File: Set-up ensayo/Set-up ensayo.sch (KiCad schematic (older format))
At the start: 14 parts, among them J1 Conn_Coaxial, J2 DB9_Female_MountingHoles

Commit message: Terminé con el 3er paso del proceso de diseño de esquemático. Cada componente tiene su footprint pero hay que vericarlo
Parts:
- H1, H2, H3, H4: footprint (none) -> MountingHole:MountingHole_2.2mm_M2_ISO7380_Pad
- J1: footprint (none) -> Connector_Coaxial:BNC_TEConnectivity_1478204_Vertical
- J2: footprint (none) -> Connector_Dsub:DSUB-9_Female_Horizontal_P2.77x2.84mm_EdgePinOffset4.94mm_Housed_MountingHolesOffset7.48mm
- MCB1: footprint (none) -> digikey-footprints:Switch_Toggle_ATE1D-2M3-10-Z
- R1: footprint (none) -> Resistor_THT:R_Axial_DIN0204_L3.6mm_D1.6mm_P5.08mm_Horizontal
- TP1, TP2, TP3, TP4, TP5, TP6: footprint (none) -> Connector_PinHeader_1.00mm:PinHeader_1x01_P1.00mm_Horizontal
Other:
- note added: "Pto. medición osciloscopio V1"
- note added: "Pto. medición osciloscopio V2"
- note removed: "Pto. medición osciloscopio"
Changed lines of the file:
@@
 F 0 "H1" H 1300 2799 50  0000 L CNN
 F 1 "MountingHole_Pad" H 1300 2708 50  0000 L CNN
-F 2 "" H 1200 2750 50  0001 C CNN
+F 2 "MountingHole:MountingHole_2.2mm_M2_ISO7380_Pad" H 1200 2750 50  0001 C CNN
 F 3 "~" H 1200 2750 50  0001 C CNN
 F 4 "Fijación e interfaz eléctrica con chasis" H 1200 2750 50  0001 C CNN "Función"
@@
 F 0 "H3" H 8400 2849 50  0000 L CNN
 F 1 "MountingHole_Pad" H 8400 2758 50  0000 L CNN
-F 2 "" H 8300 2800 50  0001 C CNN
+F 2 "MountingHole:MountingHole_2.2mm_M2_ISO7380_Pad" H 8300 2800 50  0001 C CNN
 F 3 "~" H 8300 2800 50  0001 C CNN
 F 4 "Fijación e interfaz eléctrica con chasis" H 8300 2800 50  0001 C CNN "Función"
@@
 F 0 "H2" H 1300 5149 50  0000 L CNN
 F 1 "MountingHole_Pad" H 1300 5058 50  0000 L CNN
-F 2 "" H 1200 5100 50  0001 C CNN
+F 2 "MountingHole:MountingHole_2.2mm_M2_ISO7380_Pad" H 1200 5100 50  0001 C CNN
 F 3 "~" H 1200 5100 50  0001 C CNN
 F 4 "Fijación e interfaz eléctrica con chasis" H 1200 5100 50  0001 C CNN "Función"
@@
 F 0 "H4" H 8450 5199 50  0000 L CNN
 F 1 "MountingHole_Pad" H 8450 5108 50  0000 L CNN
-F 2 "" H 8350 5150 50  0001 C CNN
+F 2 "MountingHole:MountingHole_2.2mm_M2_ISO7380_Pad" H 8350 5150 50  0001 C CNN
 F 3 "~" H 8350 5150 50  0001 C CNN
 F 4 "Fijación e interfaz eléctrica con chasis" H 8350 5150 50  0001 C CNN "Función"
@@
 F 0 "J1" H 2200 3475 50  0000 L CNN
 F 1 "Conn_Coaxial" H 2200 3384 50  0000 L CNN
-F 2 "" H 2100 3500 50  0001 C CNN
+F 2 "Connector_Coaxial:BNC_TEConnectivity_1478204_Vertical" H 2100 3500 50  0001 C CNN
 F 3 " ~" H 2100 3500 50  0001 C CNN
 F 4 "Interfaz eléctrica con generador de señales" H 2100 3500 50  0001 C CNN "Función"
@@
 F 0 "MCB1" H 4950 3825 50  0000 C CNN
 F 1 "INT_1P2D" H 4950 3734 50  0000 C CNN
-F 2 "" H 4950 3500 50  0001 C CNN
+F 2 "digikey-footprints:Switch_Toggle_ATE1D-2M3-10-Z" H 4950 3500 50  0001 C CNN
 F 3 "" H 4950 3500 50  0001 C CNN
 F 4 "Interruptor HMI para cambio enter ajuste y ensayo" H 4950 3500 50  0001 C CNN "Función"
@@
 F 0 "R1" V 5757 3400 50  0000 C CNN
 F 1 "R" V 5666 3400 50  0000 C CNN
-F 2 "" V 5480 3400 50  0001 C CNN
+F 2 "Resistor_THT:R_Axial_DIN0204_L3.6mm_D1.6mm_P5.08mm_Horizontal" V 5480 3400 50  0001 C CNN
 F 3 "~" H 5550 3400 50  0001 C CNN
 F 4 "Resistencia de medición de sensor" V 5550 3400 50  0001 C CNN "Función"
@@
 F 0 "J2" H 7680 4052 50  0000 L CNN
 F 1 "DB9_Female_MountingHoles" H 7680 3961 50  0000 L CNN
-F 2 "" H 7500 4050 50  0001 C CNN
+F 2 "Connector_Dsub:DSUB-9_Female_Horizontal_P2.77x2.84mm_EdgePinOffset4.94mm_Housed_MountingHolesOffset7.48mm" H 7500 4050 50  0001 C CNN
 F 3 " ~" H 7500 4050 50  0001 C CNN
 F 4 "Interfaz eléctrica con sensores" H 7500 4050 50  0001 C CNN "Función"
@@
 F 0 "TP3" H 3853 4001 50  0000 L CNN
 F 1 "TestPoint_Probe" H 3853 3910 50  0000 L CNN
-F 2 "" H 3900 3900 50  0001 C CNN
+F 2 "Connector_PinHeader_1.00mm:PinHeader_1x01_P1.00mm_Horizontal" H 3900 3900 50  0001 C CNN
 F 3 "~" H 3900 3900 50  0001 C CNN
 F 4 "Interfaz eléctrica con punta de medición V1 osciloscopio" H 3700 3900 50  0001 C CNN "Función"
@@
 F 0 "TP5" H 6053 3951 50  0000 L CNN
 F 1 "TestPoint_Probe" H 6053 3860 50  0000 L CNN
-F 2 "" H 6100 3850 50  0001 C CNN
+F 2 "Connector_PinHeader_1.00mm:PinHeader_1x01_P1.00mm_Horizontal" H 6100 3850 50  0001 C CNN
 F 3 "~" H 6100 3850 50  0001 C CNN
 F 4 "Interfaz eléctrica con punta de medición V2 osciloscopio" H 5900 3850 50  0001 C CNN "Función"
@@
 F 0 "TP6" H 5958 4468 50  0000 L CNN
 F 1 "TestPoint" H 5958 4377 50  0000 L CNN
-F 2 "" H 6100 4350 50  0001 C CNN
+F 2 "Connector_PinHeader_1.00mm:PinHeader_1x01_P1.00mm_Horizontal" H 6100 4350 50  0001 C CNN
 F 3 "~" H 6100 4350 50  0001 C CNN
 F 4 "Interfaz eléctrica con GND de V2 osciloscopio" H 5900 4350 50  0001 C CNN "Función"
@@
 F 0 "TP4" H 3758 4418 50  0000 L CNN
 F 1 "TestPoint" H 3758 4327 50  0000 L CNN
-F 2 "" H 3900 4300 50  0001 C CNN
+F 2 "Connector_PinHeader_1.00mm:PinHeader_1x01_P1.00mm_Horizontal" H 3900 4300 50  0001 C CNN
 F 3 "~" H 3900 4300 50  0001 C CNN
 F 4 "Interfaz eléctrica con GND de V1 osciloscopio" H 3700 4300 50  0001 C CNN "Función"
@@
 F 0 "TP1" H 2908 4068 50  0000 L CNN
 F 1 "TestPoint_Alt" H 2908 3977 50  0000 L CNN
-F 2 "" H 3050 3950 50  0001 C CNN
+F 2 "Connector_PinHeader_1.00mm:PinHeader_1x01_P1.00mm_Horizontal" H 3050 3950 50  0001 C CNN
 F 3 "~" H 3050 3950 50  0001 C CNN
 F 4 "Interfaz eléctrica con potencial positivo tester" H 2850 3950 50  0001 C CNN "Función"
@@
 F 0 "TP2" H 2908 4468 50  0000 L CNN
 F 1 "TestPoint" H 2908 4377 50  0000 L CNN
-F 2 "" H 3050 4350 50  0001 C CNN
+F 2 "Connector_PinHeader_1.00mm:PinHeader_1x01_P1.00mm_Horizontal" H 3050 4350 50  0001 C CNN
 F 3 "~" H 3050 4350 50  0001 C CNN
 F 4 "Interfaz eléctrica con potencial negativo tester" H 2850 4350 50  0001 C CNN "Función"
@@
 Pto. medición tester
 Text Notes 3600 4600 0    50   ~ 0
-Pto. medición osciloscopio
+Pto. medición osciloscopio V1
 Text Notes 4600 3900 0    50   ~ 0
 Ensayo/Ajuste
 Text Notes 5600 4600 0    50   ~ 0
-Pto. medición osciloscopio
+Pto. medición osciloscopio V2
 Wire Notes Line
 	6950 3400 6950 4750

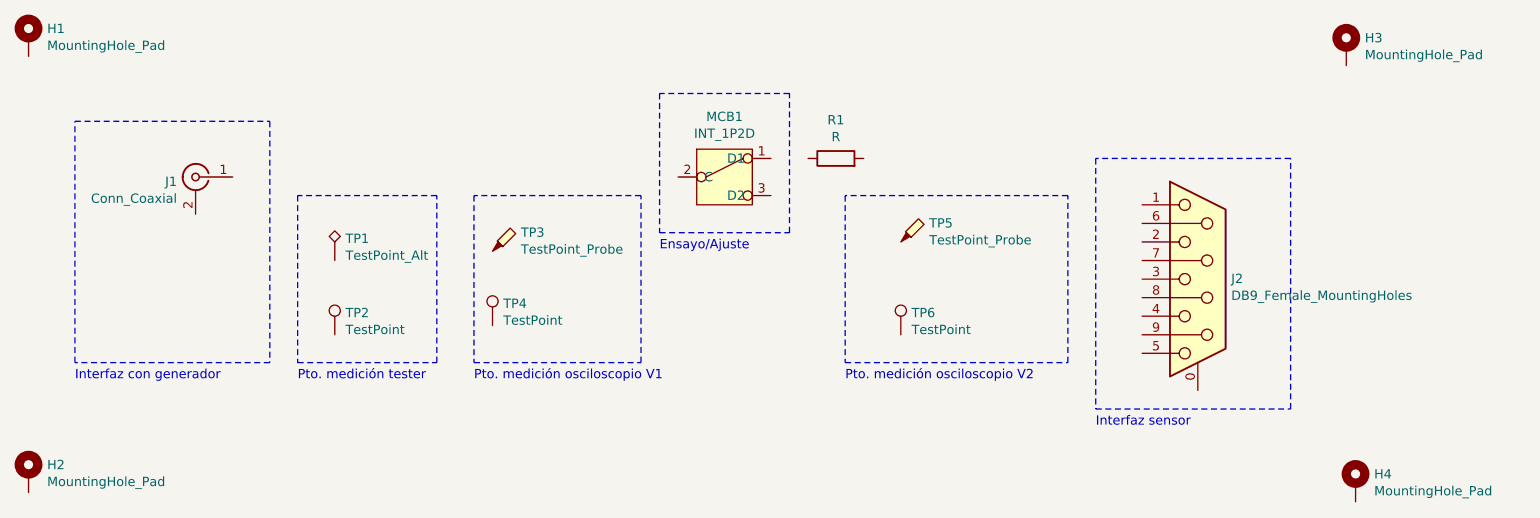
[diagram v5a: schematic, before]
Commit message: Pasos 4 y 5 del proceso de diseño de esquemático hechos
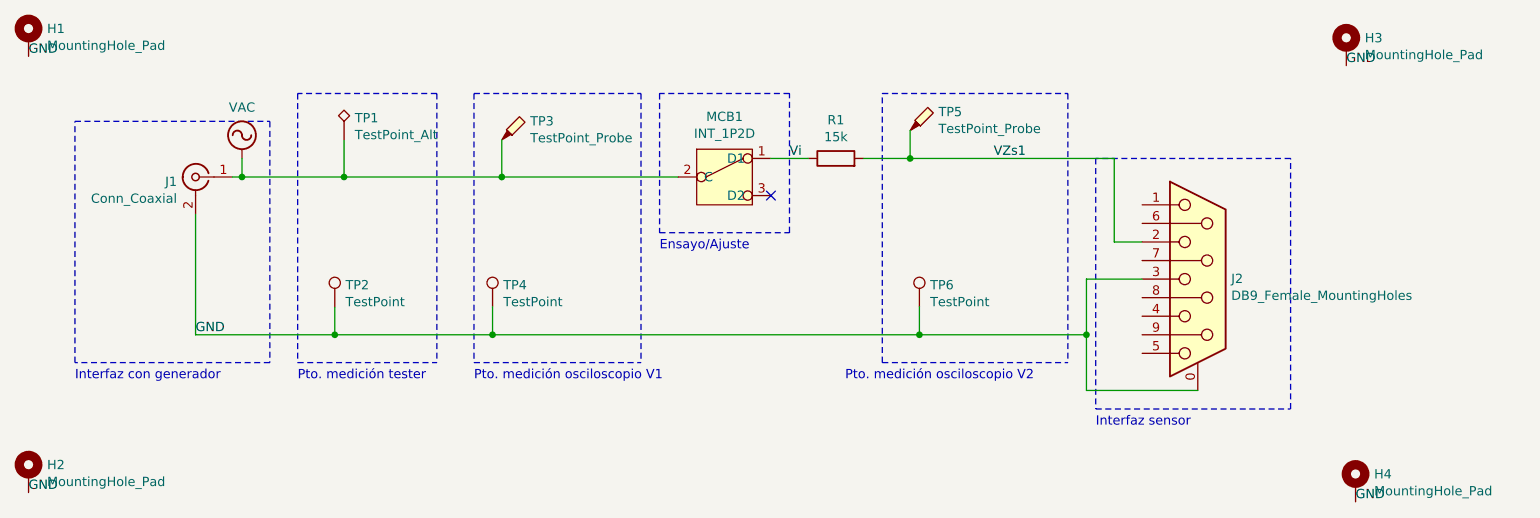
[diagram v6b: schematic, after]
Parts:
- R1: value R -> 15k
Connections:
- net GND: now reaches H1.1
- net GND: now also H2.1, H3.1, H4.1, J1.2 (Ext), J2.0 (PAD), J2.3, TP2.1, TP4.1, TP6.1
- net VAC: now reaches J1.1 (In)
- net VAC: now also MCB1.2 (C), TP1.1, TP3.1
- net Vi: now reaches MCB1.1 (D1)
- net Vi: now also R1.1
- net VZs1: now reaches R1.2
- net VZs1: now also J2.2, TP5.1
- no-connect marks 0 -> 1
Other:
- moved on the sheet: TP1, TP2, TP3, TP4, TP5, TP6
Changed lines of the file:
@@
 P 5550 3400
 F 0 "R1" V 5757 3400 50  0000 C CNN
-F 1 "R" V 5666 3400 50  0000 C CNN
+F 1 "15k" V 5666 3400 50  0000 C CNN
 F 2 "Resistor_THT:R_Axial_DIN0204_L3.6mm_D1.6mm_P5.08mm_Horizontal" V 5480 3400 50  0001 C CNN
 F 3 "~" H 5550 3400 50  0001 C CNN
@@
 L Connector:TestPoint_Probe TP3
 U 1 1 5D483898
-P 3700 3900
-F 0 "TP3" H 3853 4001 50  0000 L CNN
-F 1 "TestPoint_Probe" H 3853 3910 50  0000 L CNN
-F 2 "Connector_PinHeader_1.00mm:PinHeader_1x01_P1.00mm_Horizontal" H 3900 3900 50  0001 C CNN
-F 3 "~" H 3900 3900 50  0001 C CNN
-F 4 "Interfaz eléctrica con punta de medición V1 osciloscopio" H 3700 3900 50  0001 C CNN "Función"
-	1    3700 3900
+P 3750 3300
+F 0 "TP3" H 3903 3401 50  0000 L CNN
+F 1 "TestPoint_Probe" H 3903 3310 50  0000 L CNN
+F 2 "Connector_PinHeader_1.00mm:PinHeader_1x01_P1.00mm_Horizontal" H 3950 3300 50  0001 C CNN
+F 3 "~" H 3950 3300 50  0001 C CNN
+F 4 "Interfaz eléctrica con punta de medición V1 osciloscopio" H 3750 3300 50  0001 C CNN "Función"
+	1    3750 3300
 	1    0    0    -1
 $EndComp
@@
 L Connector:TestPoint_Probe TP5
 U 1 1 5D484196
-P 5900 3850
-F 0 "TP5" H 6053 3951 50  0000 L CNN
-F 1 "TestPoint_Probe" H 6053 3860 50  0000 L CNN
-F 2 "Connector_PinHeader_1.00mm:PinHeader_1x01_P1.00mm_Horizontal" H 6100 3850 50  0001 C CNN
-F 3 "~" H 6100 3850 50  0001 C CNN
-F 4 "Interfaz eléctrica con punta de medición V2 osciloscopio" H 5900 3850 50  0001 C CNN "Función"
-	1    5900 3850
+P 5950 3250
+F 0 "TP5" H 6103 3351 50  0000 L CNN
+F 1 "TestPoint_Probe" H 6103 3260 50  0000 L CNN
+F 2 "Connector_PinHeader_1.00mm:PinHeader_1x01_P1.00mm_Horizontal" H 6150 3250 50  0001 C CNN
+F 3 "~" H 6150 3250 50  0001 C CNN
+F 4 "Interfaz eléctrica con punta de medición V2 osciloscopio" H 5950 3250 50  0001 C CNN "Función"
+	1    5950 3250
 	1    0    0    -1
 $EndComp
@@
 L Connector:TestPoint TP6
 U 1 1 5D4852D2
-P 5900 4350
-F 0 "TP6" H 5958 4468 50  0000 L CNN
-F 1 "TestPoint" H 5958 4377 50  0000 L CNN
-F 2 "Connector_PinHeader_1.00mm:PinHeader_1x01_P1.00mm_Horizontal" H 6100 4350 50  0001 C CNN
-F 3 "~" H 6100 4350 50  0001 C CNN
-F 4 "Interfaz eléctrica con GND de V2 osciloscopio" H 5900 4350 50  0001 C CNN "Función"
-	1    5900 4350
+P 6000 4200
+F 0 "TP6" H 6058 4318 50  0000 L CNN
+F 1 "TestPoint" H 6058 4227 50  0000 L CNN
+F 2 "Connector_PinHeader_1.00mm:PinHeader_1x01_P1.00mm_Horizontal" H 6200 4200 50  0001 C CNN
+F 3 "~" H 6200 4200 50  0001 C CNN
+F 4 "Interfaz eléctrica con GND de V2 osciloscopio" H 6000 4200 50  0001 C CNN "Función"
+	1    6000 4200
 	1    0    0    -1
 $EndComp
@@
 L Connector:TestPoint TP4
 U 1 1 5D4861BC
-P 3700 4300
-F 0 "TP4" H 3758 4418 50  0000 L CNN
-F 1 "TestPoint" H 3758 4327 50  0000 L CNN
-F 2 "Connector_PinHeader_1.00mm:PinHeader_1x01_P1.00mm_Horizontal" H 3900 4300 50  0001 C CNN
-F 3 "~" H 3900 4300 50  0001 C CNN
-F 4 "Interfaz eléctrica con GND de V1 osciloscopio" H 3700 4300 50  0001 C CNN "Función"
-	1    3700 4300
+P 3700 4200
+F 0 "TP4" H 3758 4318 50  0000 L CNN
+F 1 "TestPoint" H 3758 4227 50  0000 L CNN
+F 2 "Connector_PinHeader_1.00mm:PinHeader_1x01_P1.00mm_Horizontal" H 3900 4200 50  0001 C CNN
+F 3 "~" H 3900 4200 50  0001 C CNN
+F 4 "Interfaz eléctrica con GND de V1 osciloscopio" H 3700 4200 50  0001 C CNN "Función"
+	1    3700 4200
 	1    0    0    -1
 $EndComp
@@
 L Connector:TestPoint_Alt TP1
 U 1 1 5D486AED
-P 2850 3950
-F 0 "TP1" H 2908 4068 50  0000 L CNN
-F 1 "TestPoint_Alt" H 2908 3977 50  0000 L CNN
-F 2 "Connector_PinHeader_1.00mm:PinHeader_1x01_P1.00mm_Horizontal" H 3050 3950 50  0001 C CNN
-F 3 "~" H 3050 3950 50  0001 C CNN
-F 4 "Interfaz eléctrica con potencial positivo tester" H 2850 3950 50  0001 C CNN "Función"
-	1    2850 3950
+P 2900 3300
+F 0 "TP1" H 2958 3418 50  0000 L CNN
+F 1 "TestPoint_Alt" H 2958 3327 50  0000 L CNN
+F 2 "Connector_PinHeader_1.00mm:PinHeader_1x01_P1.00mm_Horizontal" H 3100 3300 50  0001 C CNN
+F 3 "~" H 3100 3300 50  0001 C CNN
+F 4 "Interfaz eléctrica con potencial positivo tester" H 2900 3300 50  0001 C CNN "Función"
+	1    2900 3300
 	1    0    0    -1
 $EndComp
@@
 L Connector:TestPoint TP2
 U 1 1 5D487102
-P 2850 4350
-F 0 "TP2" H 2908 4468 50  0000 L CNN
-F 1 "TestPoint" H 2908 4377 50  0000 L CNN
-F 2 "Connector_PinHeader_1.00mm:PinHeader_1x01_P1.00mm_Horizontal" H 3050 4350 50  0001 C CNN
-F 3 "~" H 3050 4350 50  0001 C CNN
-F 4 "Interfaz eléctrica con potencial negativo tester" H 2850 4350 50  0001 C CNN "Función"
-	1    2850 4350
+P 2850 4200
+F 0 "TP2" H 2908 4318 50  0000 L CNN
+F 1 "TestPoint" H 2908 4227 50  0000 L CNN
+F 2 "Connector_PinHeader_1.00mm:PinHeader_1x01_P1.00mm_Horizontal" H 3050 4200 50  0001 C CNN
+F 3 "~" H 3050 4200 50  0001 C CNN
+F 4 "Interfaz eléctrica con potencial negativo tester" H 2850 4200 50  0001 C CNN "Función"
+	1    2850 4200
 	1    0    0    -1
 $EndComp
@@
 	1450 4500 1450 3200
 Wire Notes Line
-	2650 3600 2650 4500
-Wire Notes Line
 	2650 4500 3400 4500
 Wire Notes Line
-	3400 4500 3400 3600
-Wire Notes Line
-	3400 3600 2650 3600
-Wire Notes Line
-	3600 3600 3600 4500
-Wire Notes Line
 	3600 4500 4500 4500
 Wire Notes Line
-	4500 4500 4500 3600
-Wire Notes Line
-	4500 3600 3600 3600
-Wire Notes Line
 	4600 3050 4600 3800
 Wire Notes Line
@@
 Wire Notes Line
 	5300 3050 4600 3050
-Wire Notes Line
-	5600 3600 5600 4500
-Wire Notes Line
-	5600 4500 6800 4500
-Wire Notes Line
-	6800 4500 6800 3600
-Wire Notes Line
-	6800 3600 5600 3600
 Text Notes 1450 4600 0    50   ~ 0
 Interfaz con generador
@@
 Text Notes 6950 4850 0    50   ~ 0
 Interfaz sensor
+Wire Wire Line
+	2300 3500 2350 3500
+Wire Wire Line
+	2900 3300 2900 3500
+Connection ~ 2900 3500
+Wire Wire Line
+	2900 3500 3750 3500
+Wire Wire Line
+	3750 3300 3750 3500
+Connection ~ 3750 3500
+Wire Wire Line
+	3750 3500 4700 3500
+Wire Wire Line
+	2100 3700 2100 4350
+Wire Wire Line
+	2100 4350 2850 4350
+Wire Wire Line
+	2850 4350 3700 4350
+Connection ~ 2850 4350
+Wire Wire Line
+	6000 4350 6900 4350
+Wire Wire Line
+	6900 4350 6900 4650
+Wire Wire Line
+	6900 4650 7500 4650
+Connection ~ 6000 4350
+Wire Wire Line
+	7200 4050 6900 4050
+Wire Wire Line
+	6900 4050 6900 4350
+Connection ~ 6900 4350
+Wire Wire Line
+	5400 3400 5200 3400
+Wire Wire Line
+	5700 3400 5950 3400
+Wire Wire Line
+	7050 3400 7050 3850
+Wire Wire Line
+	7050 3850 7200 3850
+NoConn ~ 5200 3600
+Wire Wire Line
+	5950 3250 5950 3400
+Connection ~ 5950 3400
+Wire Wire Line
+	5950 3400 7050 3400
+Wire Wire Line
+	3700 4200 3700 4350
+Connection ~ 3700 4350
+Wire Wire Line
+	3700 4350 6000 4350
+Wire Notes Line
+	5800 4500 5800 3050
+Wire Notes Line
+	5800 3050 6800 3050
+Wire Notes Line
+	6800 3050 6800 4500
+Wire Notes Line
+	5800 4500 6800 4500
+Wire Wire Line
+	6000 4200 6000 4350
+Wire Notes Line
+	3600 3050 4500 3050
+Wire Notes Line
+	3600 3050 3600 4500
+Wire Notes Line
+	4500 3050 4500 4500
+Wire Notes Line
+	3400 3050 2650 3050
+Wire Notes Line
+	2650 3050 2650 4500
+Wire Notes Line
+	3400 3050 3400 4500
+Text Label 2100 4350 0    50   ~ 0
+GND
+Text Label 6400 3400 0    50   ~ 0
+VZs1
+Text Label 1200 2850 0    50   ~ 0
+GND
+Text Label 1200 5200 0    50   ~ 0
+GND
+Text Label 8350 5250 0    50   ~ 0
+GND
+Text Label 8300 2900 0    50   ~ 0
+GND
+$Comp
+L power:VAC #PWR?
+U 1 1 5D4B4B6A
+P 2350 3400
+F 0 "#PWR?" H 2350 3300 50  0001 C CNN
+F 1 "VAC" H 2350 3675 50  0000 C CNN
+F 2 "" H 2350 3400 50  0001 C CNN
+F 3 "" H 2350 3400 50  0001 C CNN
+	1    2350 3400
+	1    0    0    -1
+$EndComp
+Connection ~ 2350 3500
+Wire Wire Line
+	2350 3500 2900 3500
+Text Label 5300 3400 0    50   ~ 0
+Vi
+Wire Wire Line
+	2850 4200 2850 4350
+Wire Wire Line
+	2350 3400 2350 3500
 $EndSCHEMATC

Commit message: Paso 6 (ERC) de proceso de diseño de esquemático hecho
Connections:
- no-connect marks 1 -> 8
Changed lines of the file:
@@
 Interfaz sensor
-Wire Wire Line
-	2300 3500 2350 3500
 Wire Wire Line
 	2900 3300 2900 3500
@@
 Text Label 8300 2900 0    50   ~ 0
 GND
-$Comp
-L power:VAC #PWR?
-U 1 1 5D4B4B6A
-P 2350 3400
-F 0 "#PWR?" H 2350 3300 50  0001 C CNN
-F 1 "VAC" H 2350 3675 50  0000 C CNN
-F 2 "" H 2350 3400 50  0001 C CNN
-F 3 "" H 2350 3400 50  0001 C CNN
-	1    2350 3400
-	1    0    0    -1
-$EndComp
-Connection ~ 2350 3500
-Wire Wire Line
-	2350 3500 2900 3500
 Text Label 5300 3400 0    50   ~ 0
 Vi
 Wire Wire Line
 	2850 4200 2850 4350
+NoConn ~ 7200 3650
+NoConn ~ 7200 3750
+NoConn ~ 7200 3950
+NoConn ~ 7200 4150
+NoConn ~ 7200 4250
+NoConn ~ 7200 4350
+NoConn ~ 7200 4450
 Wire Wire Line
-	2350 3400 2350 3500
+	2300 3500 2900 3500
+Text Label 2400 3500 0    50   ~ 0
+VAC
 $EndSCHEMATC
